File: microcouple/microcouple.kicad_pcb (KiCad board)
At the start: 4 copper layers, 29.5 x 34.2 mm, 132 parts, among them J1 Conn_ARM_SWD_TagConnect_TC203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, J2 USB_C_Socket, J4 Conn_02x03_Odd_Even, Q1 AO3415, SW1 ~{RESET}, SW2 SW_SPDT_MSK12CO2, U1 USBLC6-2SC6, U2 RP2040, U3 MCP73831-2-OT, U4 LM3671MFX, U5 IS31FL3729, U6 CAP1188, U7 IRM-V838M3-C/TR1, X1 12MHz 12pF

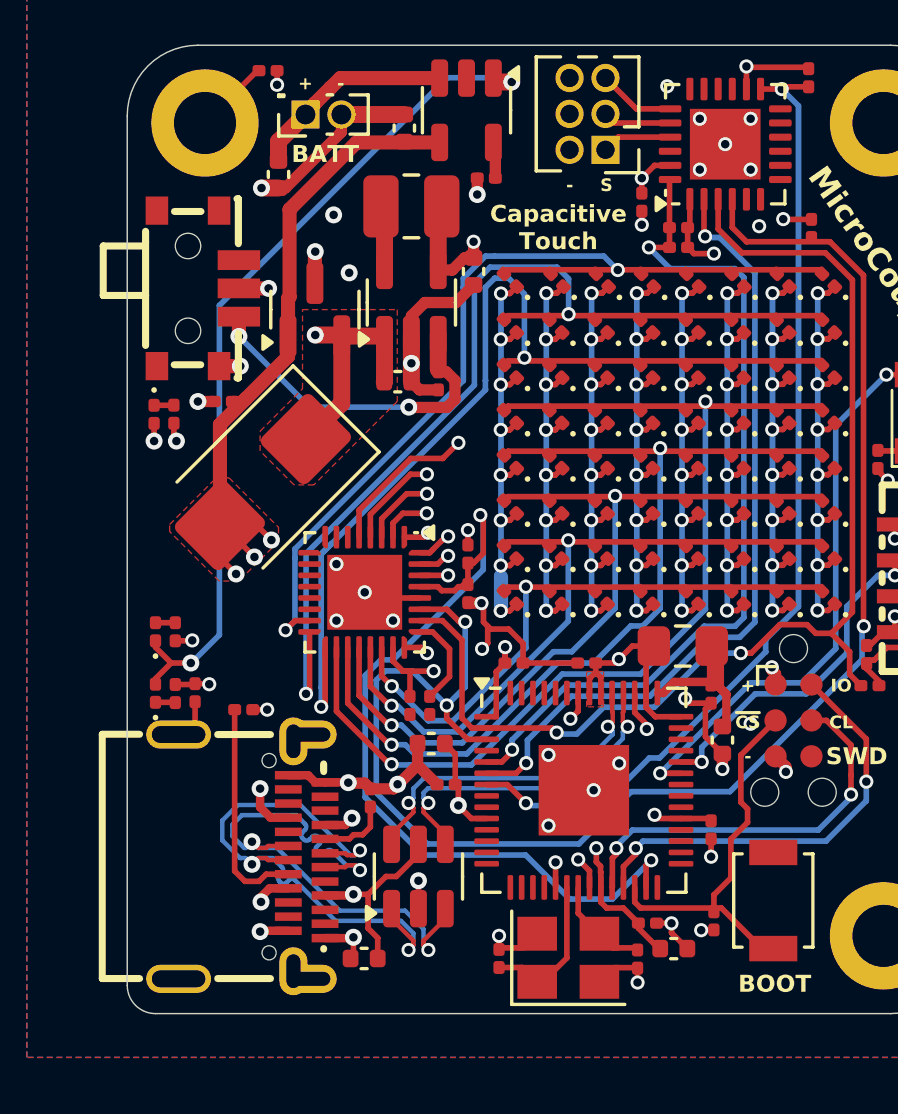
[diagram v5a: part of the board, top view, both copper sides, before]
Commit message: Update for JLCPCB
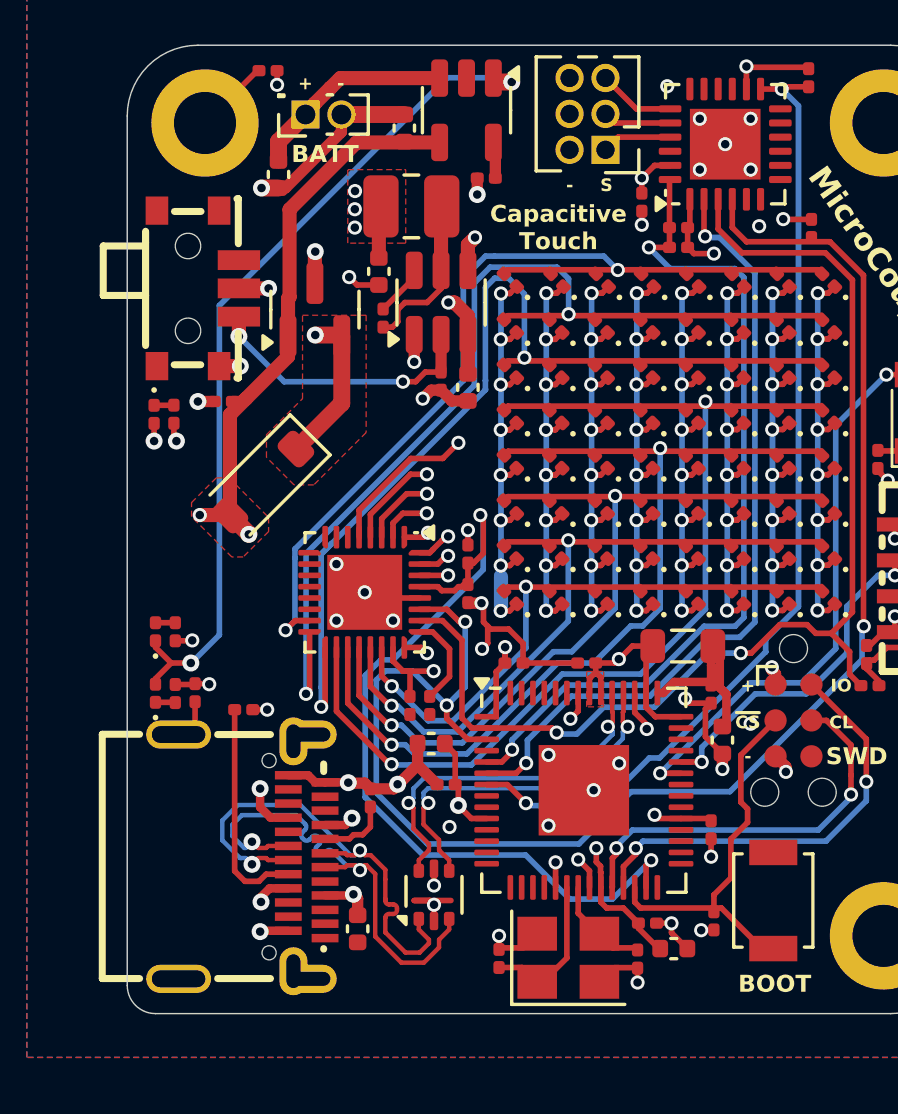
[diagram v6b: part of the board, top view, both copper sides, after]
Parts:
- added C27: 100nF, GS_Capacitors:C_0201_0603Metric, F.Cu at (95.2, 54.2)
- BT1: value 3.7V LiPo -> 4.2V LiPo
- C1, C11, C13, C14, C15, C17, C8, C9: footprint GS_SMD:0402_1005Metric -> GS_Capacitors:C_0402_1005Metric
- C10, C12, C16, C18, C19, C2, C20, C21, C22, C23, C24, C25, C26, C5, C6, C7: footprint GS_SMD:0201_0603Metric -> GS_Capacitors:C_0201_0603Metric
- C3, C4: value 14 pF -> 14pF; footprint GS_SMD:0201_0603Metric -> GS_Capacitors:C_0201_0603Metric
- D1: value GREEN -> Green
- D10, D11, D12, D13, D14, D15, D16, D17, D18, D19, D20, D21, D22, D23, D24, D25, D26, D27, D28, D29, D30, D31, D32, D33, D34, D35, D36, D37, D38, D39, D40, D41, D42, D43, D44, D45, D46, D47, D48, D49, D5, D50, D51, D52, D53, D54, D55, D56, D57, D58, D59, D6, D60, D61, D62, D63, D64, D65, D66, D67, D68, D7, D8, D9: value RED -> Red
- D2: value SB5H100 -> 40V 1A; footprint Diode_SMD:D_SMB -> Diode_SMD:D_SOD-123
- D3: value Charging -> Red
- D4: value Done -> Green
- FB1: footprint Inductor_SMD:L_0805_2012Metric_Pad1.15x1.40mm_HandSolder -> Inductor_SMD:L_0805_2012Metric
- H1, H2, H3: value MountingHole_Pad -> M2
- R1, R10, R11, R12, R13, R14, R15, R16, R17, R2, R3, R6, R7, R8, R9: footprint GS_SMD:0201_0603Metric -> GS_Resistors:R_0201_0603Metric
- SW1: value ~{RESET} -> SW_Push
- SW2: value SW_SPDT_MSK12CO2 -> MSK12CO2
- U1: value USBLC6-2SC6 -> USBLC6-2P6-MS; footprint Package_TO_SOT_SMD:SOT-23-6 -> Package_TO_SOT_SMD:SOT-666
- U3: value MCP73831-2-OT -> MCP73831
- U4: value LM3671MFX -> AP63203WU-7; footprint Package_TO_SOT_SMD:TSOT-23-5 -> Package_TO_SOT_SMD:TSOT-23-6
- moved C17 3.35 mm to (95.0, 52.6)
- moved C15 2.49 mm to (98.2, 56.7), turned to -90 degrees
- moved C1 1.07 mm to (94.3, 75.8), turned to -90 degrees
- moved U4 1.05 mm to (97.2, 53.7)
- moved U1 0.85 mm to (97.0, 74.7)
- moved C16 0.10 mm to (97.2, 56.5)
- turned L1 to 180 degrees
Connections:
- U4 pad 1: /Battery Management/VIN -> +3.3V
- U4 pad 2: GND -> /Battery Management/PWR_ENABLE
- U4 pad 3: /Battery Management/PWR_ENABLE -> /Battery Management/VIN
- U4 pad 4: +3.3V -> GND
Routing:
- net VBUS: track 33.2 -> 27.7 mm
- net /Battery Management/VIN: track 11.7 -> 16.6 mm, vias 2 -> 3
- net Net-(U4-SW): track 2.14 -> 5.78 mm
- net /USB.D-: track 20.3 -> 17.7 mm, vias 3 -> 2
- net /USB.D+: track 20.4 -> 17.7 mm, vias 3 -> 2
- net Net-(U4-BST): track 0.00 -> 1.82 mm
- net GND: track 54.0 -> 52.2 mm, vias 52 -> 51
- net /USB.D_PROTECTED+: track 11.5 -> 12.9 mm
- net /USB.D_PROTECTED-: track 11.5 -> 12.9 mm
- net /Battery Management/PWR_ENABLE: track 12.1 -> 11.3 mm
- net +3.3V: track 37.4 -> 36.9 mm, vias 14 -> 17
- net (no net): vias 0 -> 1

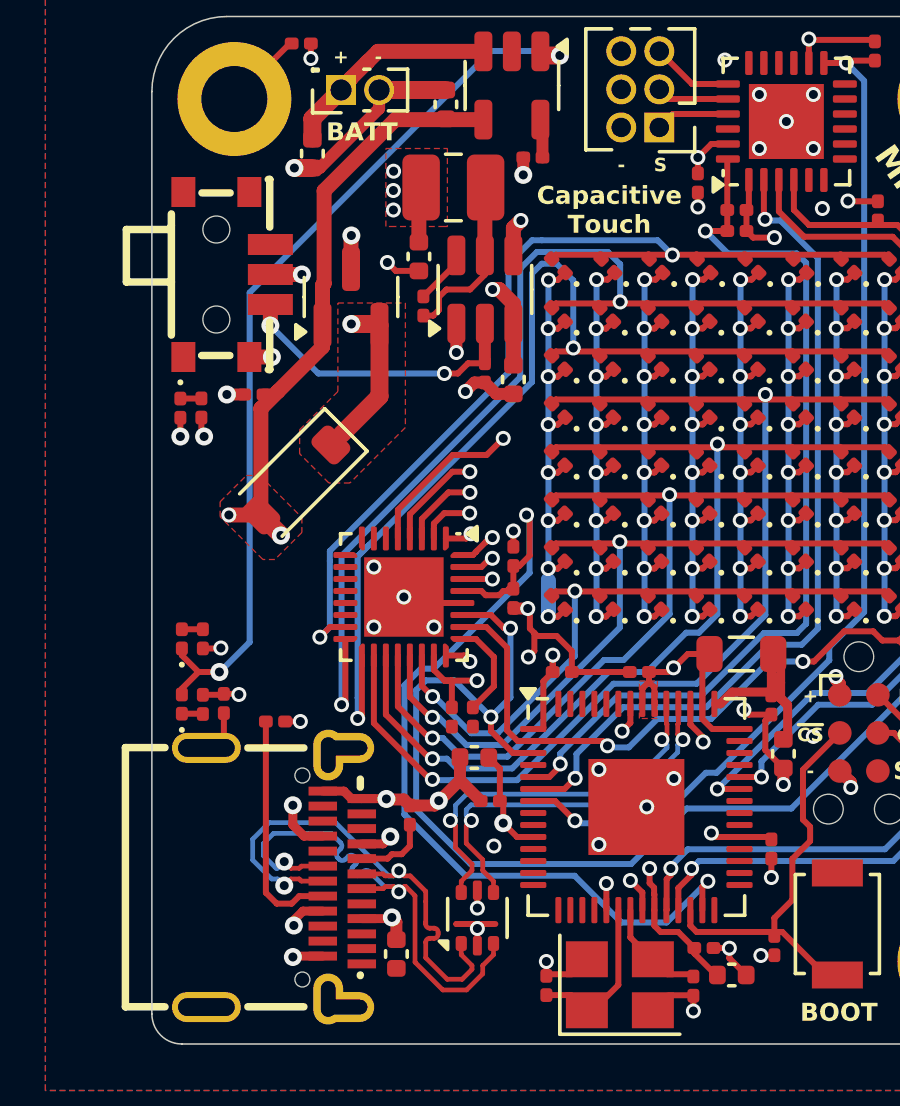
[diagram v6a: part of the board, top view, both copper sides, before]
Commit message: Change missing part on JLC
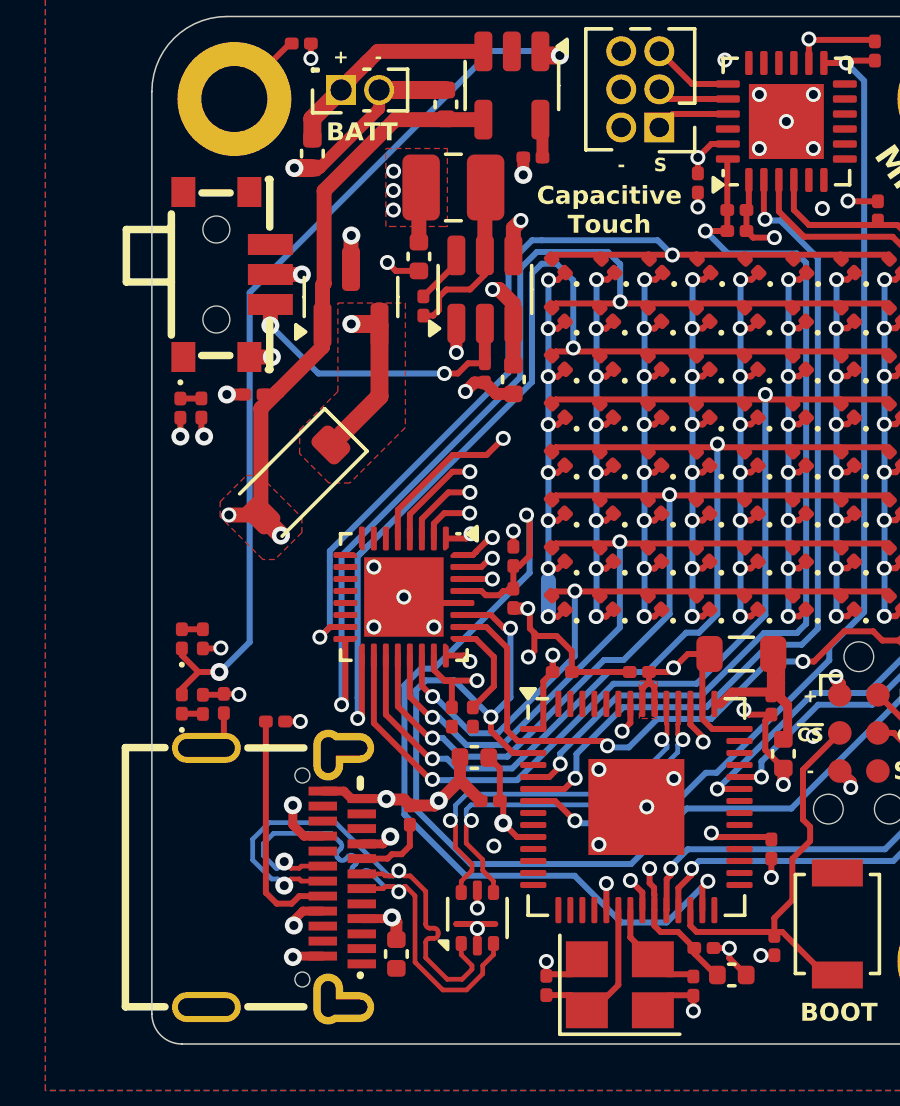
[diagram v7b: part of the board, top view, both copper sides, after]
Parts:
- BT1: value 4.2V LiPo -> Battery_Cell
- H1, H2, H3: value M2 -> MountingHole_Pad
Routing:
- net +3.3V: track 36.9 -> 36.0 mm

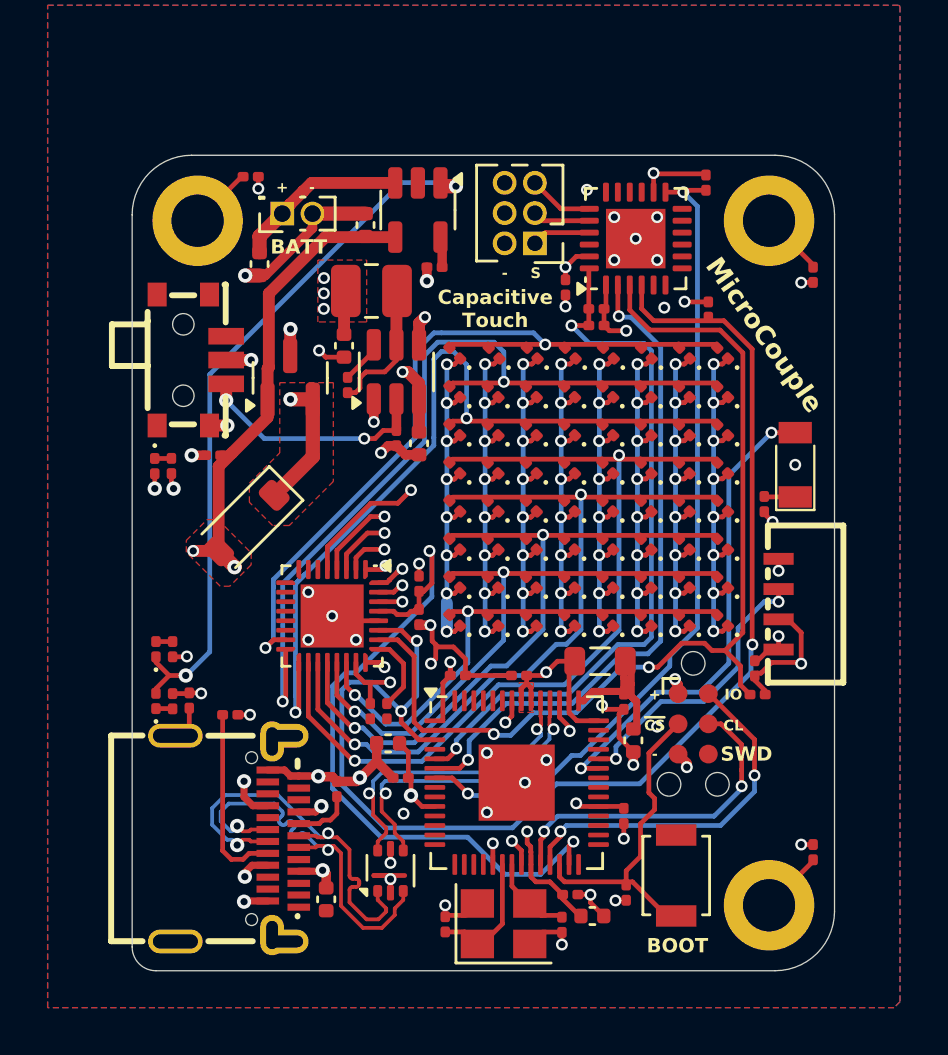
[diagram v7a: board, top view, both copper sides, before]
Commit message: Change all components to 0402 if smaller
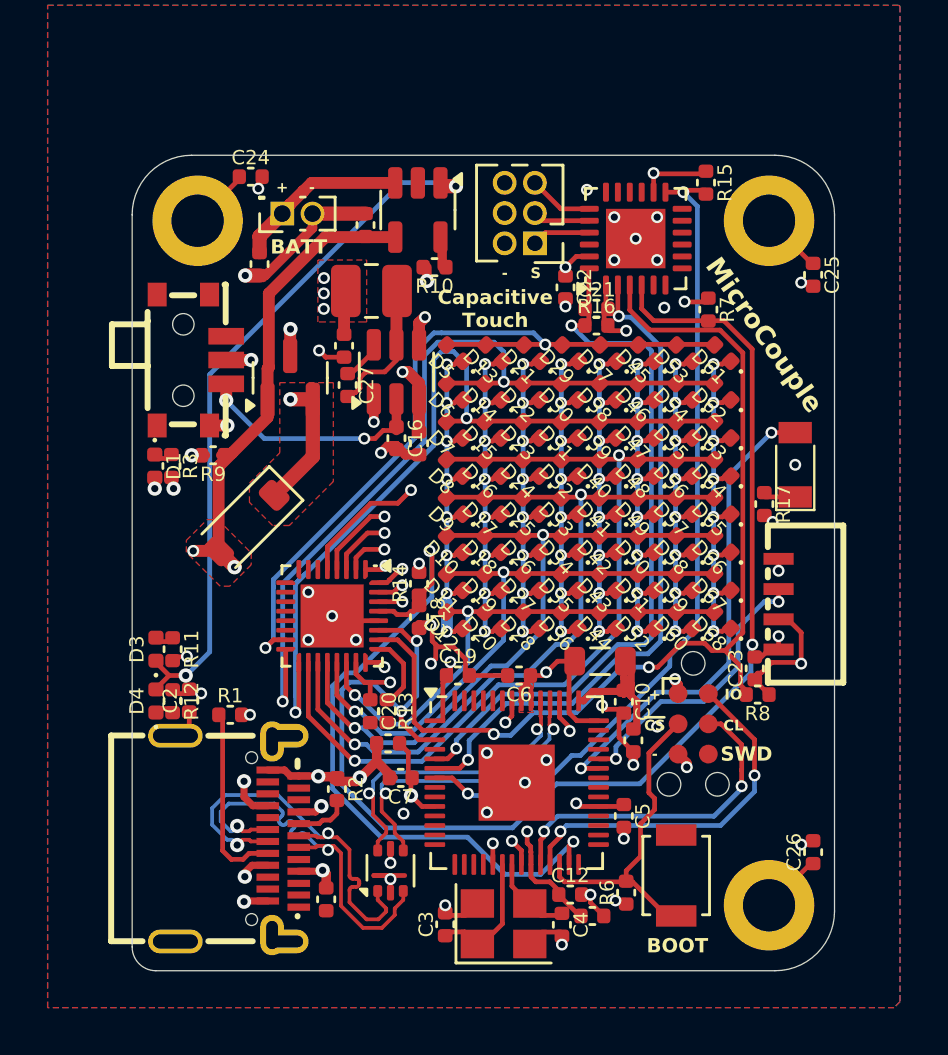
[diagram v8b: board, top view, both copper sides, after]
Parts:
- C10, C12, C16, C18, C19, C2, C20, C21, C22, C23, C24, C25, C26, C27, C3, C4, C5, C6, C7: footprint GS_Capacitors:C_0201_0603Metric -> GS_Capacitors:C_0402_1005Metric
- D1, D10, D11, D12, D13, D14, D15, D16, D17, D18, D19, D20, D21, D22, D23, D24, D25, D26, D27, D28, D29, D3, D30, D31, D32, D33, D34, D35, D36, D37, D38, D39, D4, D40, D41, D42, D43, D44, D45, D46, D47, D48, D49, D5, D50, D51, D52, D53, D54, D55, D56, D57, D58, D59, D6, D60, D61, D62, D63, D64, D65, D66, D67, D68, D7, D8, D9: footprint GS_Optoelectronics:LED_0201_0603Metric -> GS_Optoelectronics:LED_0402_1005Metric
- R1, R10, R11, R12, R13, R14, R15, R16, R17, R2, R3, R6, R7, R8, R9: footprint GS_Resistors:R_0201_0603Metric -> GS_Resistors:R_0402_1005Metric
